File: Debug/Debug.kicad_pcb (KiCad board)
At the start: 4 copper layers, 127 x 88.9 mm, 37 parts, among them J1 Expansion_Connector, SW1 Step, SW2 PHI1/Step, SW3 Run, SW4 SI/SC, U1 74LS04, U10 MC14495P1, U11 HDSP-7803, U12 MC14495P1, U13 HDSP-7803, U14 MC14495P1, U15 HDSP-7803, U2 74LS74, U3 MC14495P1, U4 HDSP-7803, U5 74LS374, U6 MC14495P1, U7 HDSP-7803, U8 MC14495P1, U9 HDSP-7803

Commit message: 98 unrouted traces...
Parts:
- U1: value 74LS04 -> 74HCT04
- U2: value 74LS74 -> 74HCT74
- U5: value 74LS374 -> 74HCT374
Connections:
- J1 pad 1: VCC -> +5V
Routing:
- net GND: track 0.00 -> 601.5 mm
- net ~{IRQ}: track 0.00 -> 60.2 mm, vias 0 -> 2
- net +5V: track 0.00 -> 57.0 mm
- net LE: track 0.00 -> 49.0 mm
- net Net-(SW3-Pad1): track 0.00 -> 14.0 mm
- net Net-(D5-Pad2): track 0.00 -> 7.63 mm, vias 0 -> 1
- net Net-(D4-Pad2): track 0.00 -> 7.63 mm, vias 0 -> 1
- net Net-(D8-Pad2): track 0.00 -> 7.63 mm, vias 0 -> 1
- net Net-(D1-Pad2): track 0.00 -> 7.62 mm, vias 0 -> 1
- net Net-(D6-Pad2): track 0.00 -> 7.62 mm, vias 0 -> 1
- net Net-(D3-Pad2): track 0.00 -> 7.62 mm, vias 0 -> 1
- net Net-(D7-Pad2): track 0.00 -> 7.62 mm, vias 0 -> 1
- net Net-(D2-Pad2): track 0.00 -> 7.62 mm, vias 0 -> 1
- net Net-(SW1-Pad2): track 0.00 -> 6.00 mm
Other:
- outline, holes or cut-outs redrawn

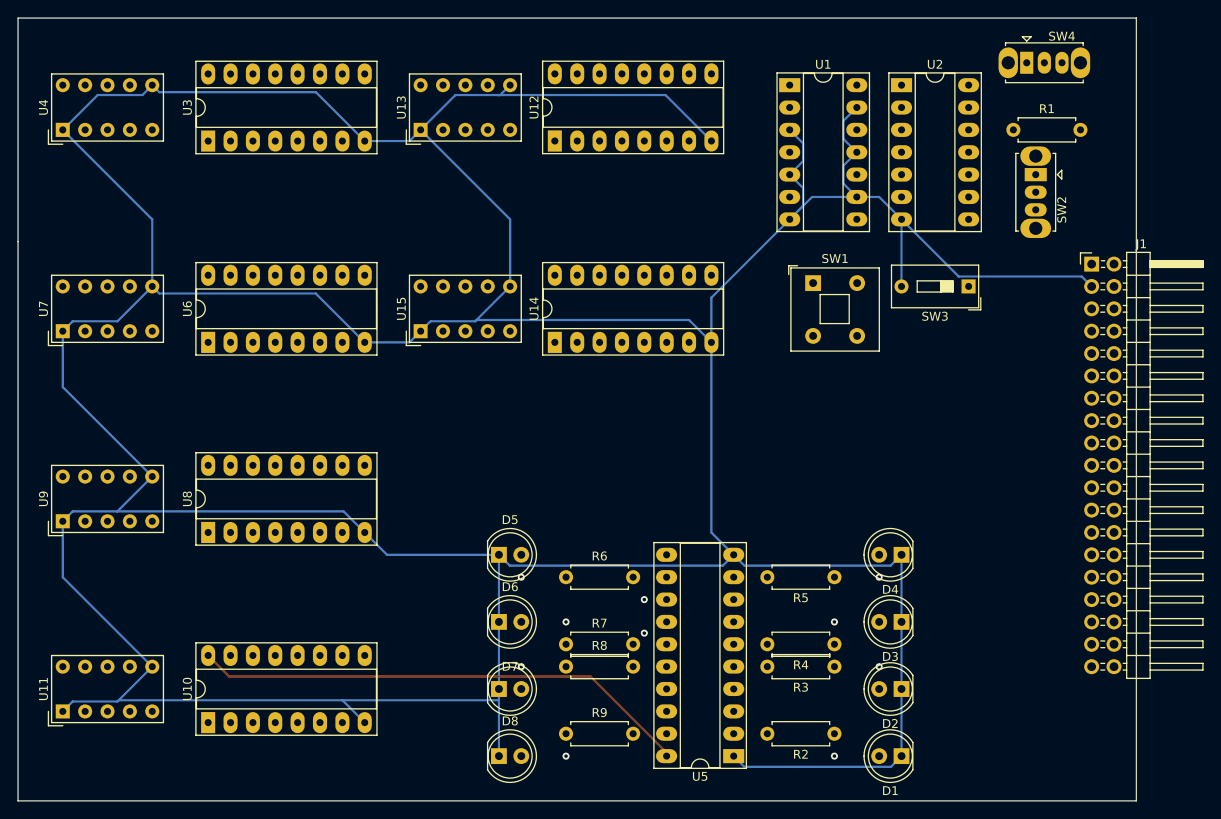
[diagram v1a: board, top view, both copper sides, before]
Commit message: 90 unrouted traces...
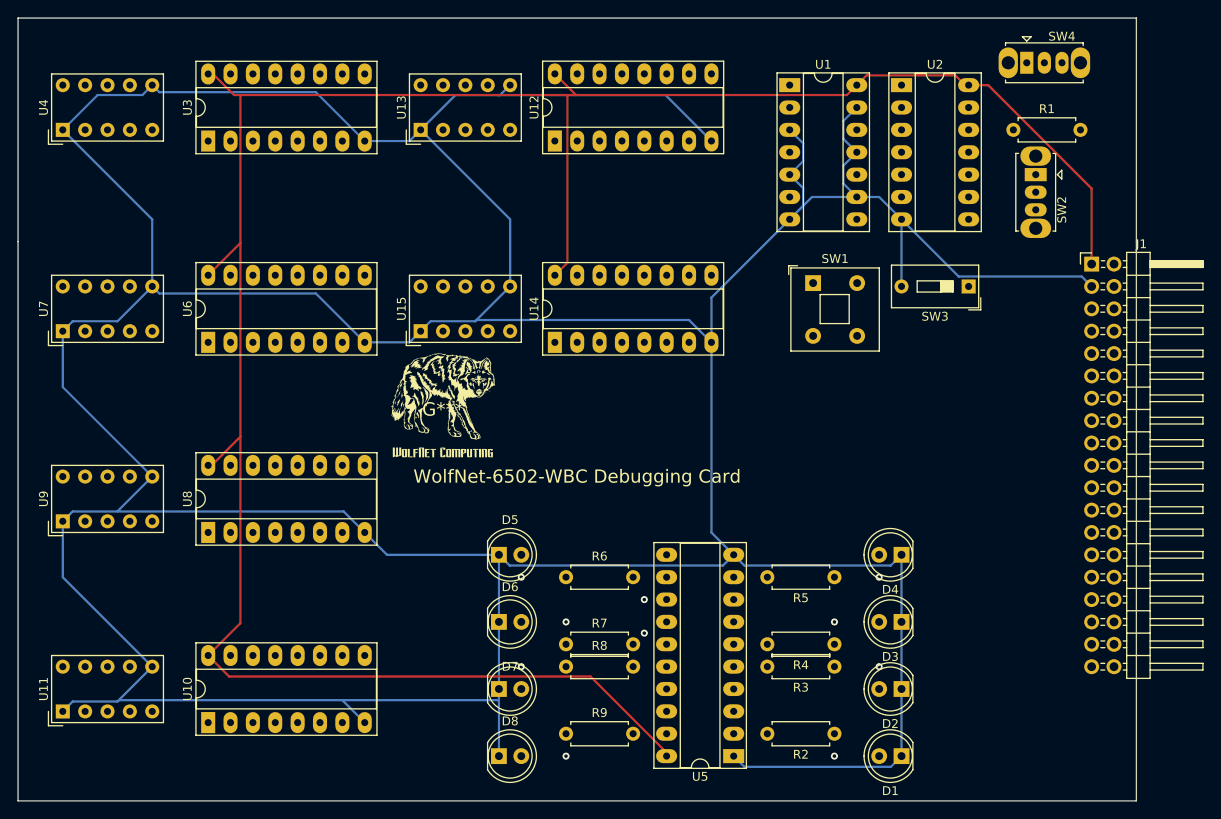
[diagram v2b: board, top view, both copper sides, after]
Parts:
- added G***: LOGO, WolfNet:WolfNet-Logo_silkscreen, F.Cu at (124.5, 69.8)
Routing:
- net +5V: track 57.0 -> 273.0 mm
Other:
- board text added: "WolfNet-6502-WBC Debugging Card"

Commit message: 64 unrouted traces...
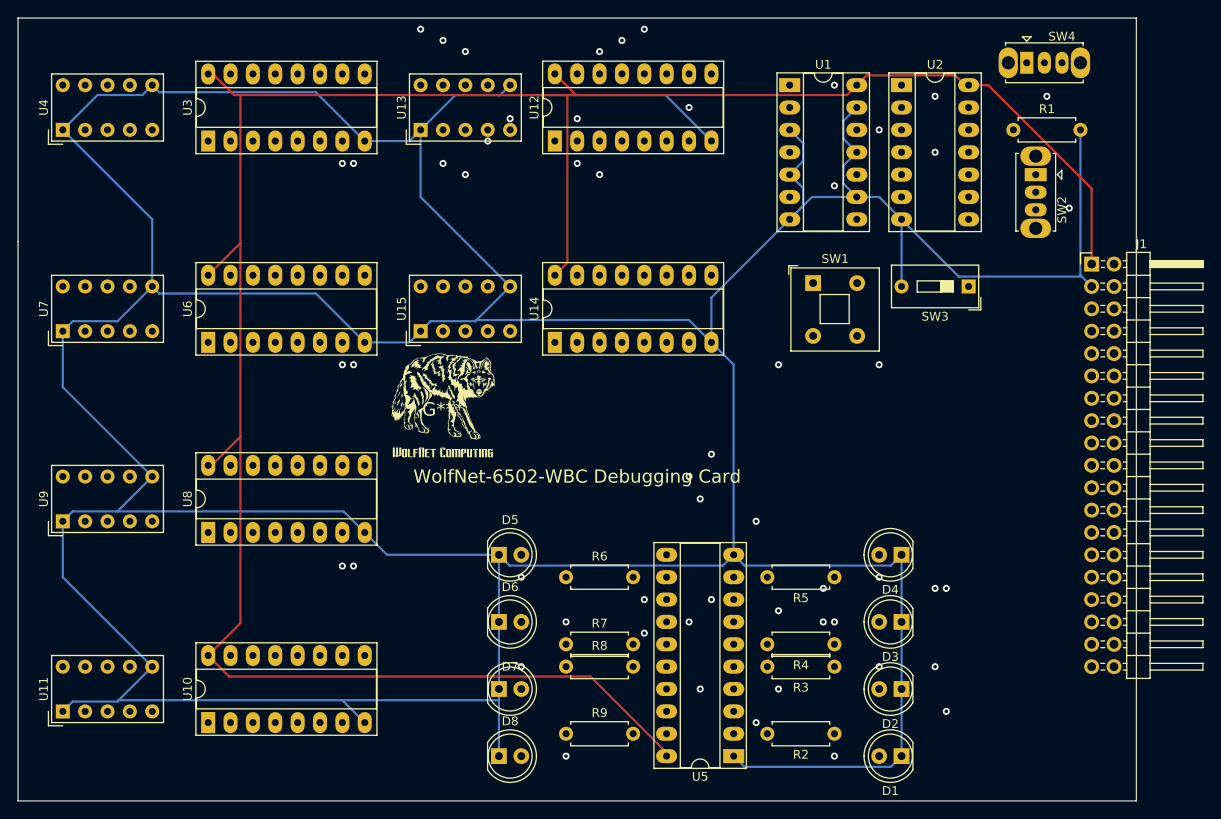
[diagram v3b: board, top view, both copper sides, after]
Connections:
- J1 pad 37: R\~{W} -> R/~{W}
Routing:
- net LE: track 49.0 -> 177.0 mm, vias 0 -> 7
- net SYNC: track 0.00 -> 121.9 mm, vias 0 -> 5
- net PHI1: track 0.00 -> 82.3 mm, vias 0 -> 2
- net PHI2: track 0.00 -> 76.2 mm, vias 0 -> 2
- net CLK: track 0.00 -> 68.6 mm, vias 0 -> 2
- net ~{RESET}: track 0.00 -> 66.0 mm, vias 0 -> 2
- net RDY: track 0.00 -> 58.4 mm, vias 0 -> 2
- net R/~{W}: track 0.00 -> 53.4 mm, vias 0 -> 4
- net Net-(SW2-Pad2): track 0.00 -> 39.7 mm, vias 0 -> 2
- net Net-(U12-Pad12): track 0.00 -> 36.8 mm, vias 0 -> 2
- net Net-(U12-Pad13): track 0.00 -> 29.2 mm, vias 0 -> 2
- net Step: track 0.00 -> 28.8 mm, vias 0 -> 1
- net Net-(SW4-Pad2): track 0.00 -> 26.8 mm, vias 0 -> 3
- net Net-(U12-Pad3): track 0.00 -> 24.1 mm, vias 0 -> 2
- net Net-(U12-Pad2): track 0.00 -> 21.6 mm, vias 0 -> 2
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
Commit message: 59 unrouted traces...
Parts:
- SW3: footprint Button_Switch_THT:SW_DIP_SPSTx01_Slide_9.78x4.72mm_W7.62mm_P2.54mm -> Button_Switch_THT:SW_Slide_1P2T_CK_OS102011MS2Q
- moved SW3 0.73 mm to (184.9, 55.9)
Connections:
- SW3 pad 1: Net-(SW3-Pad1) -> unconnected-(SW3-Pad1)
- SW3 pad 2: GND -> Net-(U2-Pad10)
- U2 pad 10: Net-(SW3-Pad1) -> Net-(U2-Pad10)
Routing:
- net A15: track 0.00 -> 86.8 mm
- net RDY: track 58.4 -> 115.6 mm, vias 2 -> 7
- net Net-(R1-Pad1): track 5.08 -> 45.8 mm, vias 0 -> 4
- net Net-(SW1-Pad1): track 0.00 -> 37.8 mm, vias 0 -> 3
- net Net-(SW1-Pad2): track 6.00 -> 20.8 mm, vias 0 -> 1
- net Net-(SW3-Pad1): track 14.0 -> 0.00 mm
- net Net-(U2-Pad10): track 0.00 -> 13.4 mm
- net GND: track 618.2 -> 613.6 mm

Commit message: 45 unrouted traces...
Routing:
- net D3: track 0.00 -> 89.8 mm, vias 0 -> 3
- net D2: track 0.00 -> 84.2 mm, vias 0 -> 3
- net Net-(U3-Pad12): track 0.00 -> 38.1 mm, vias 0 -> 2
- net PHI1: track 82.3 -> 119.2 mm, vias 2 -> 4
- net Net-(U3-Pad13): track 0.00 -> 30.5 mm, vias 0 -> 2
- net Net-(U3-Pad3): track 0.00 -> 27.9 mm, vias 0 -> 2
- net Net-(U6-Pad3): track 0.00 -> 25.4 mm, vias 0 -> 2
- net Net-(U3-Pad2): track 0.00 -> 25.4 mm, vias 0 -> 2
- net Net-(U3-Pad14): track 0.00 -> 22.9 mm, vias 0 -> 2
- net Net-(U6-Pad2): track 0.00 -> 22.9 mm, vias 0 -> 2
- net Net-(U6-Pad15): track 0.00 -> 15.2 mm, vias 0 -> 2
- net Net-(U3-Pad15): track 0.00 -> 15.2 mm, vias 0 -> 2
- net Net-(U3-Pad1): track 0.00 -> 15.2 mm, vias 0 -> 2
- net Net-(U6-Pad1): track 0.00 -> 10.2 mm, vias 0 -> 1
- net +5V: track 271.3 -> 278.1 mm
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
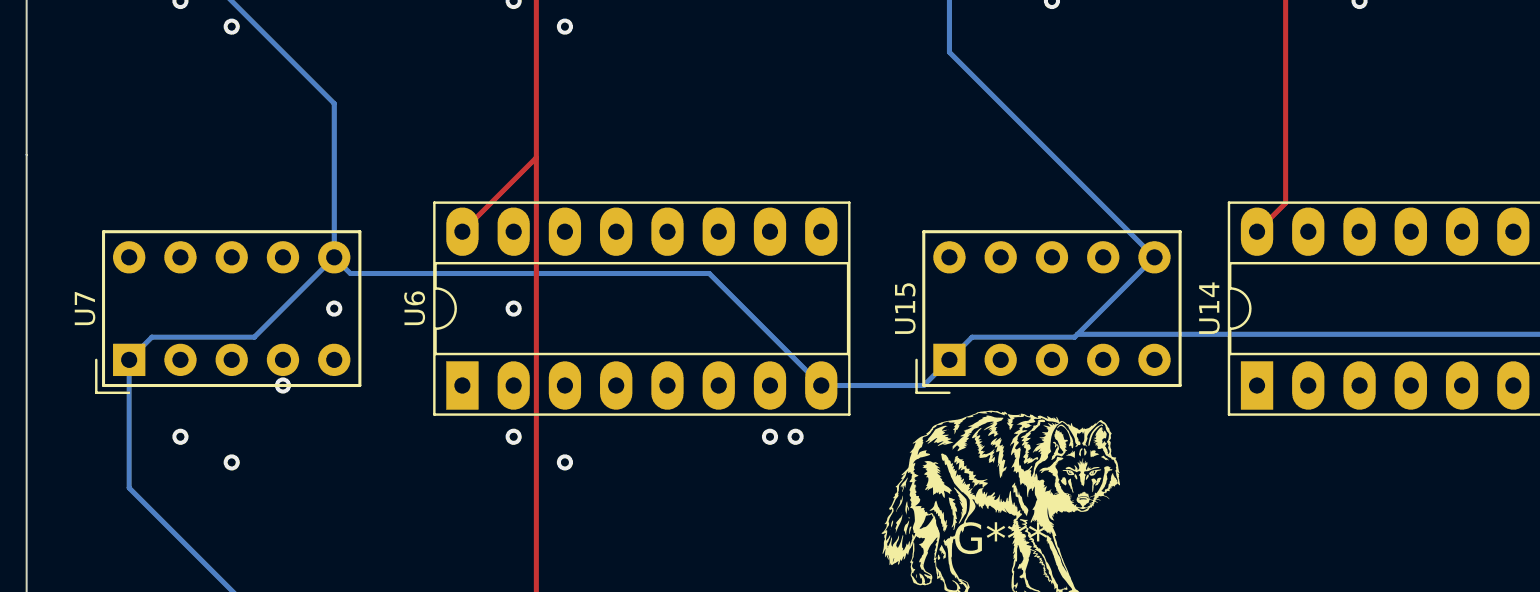
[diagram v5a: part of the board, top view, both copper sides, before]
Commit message: 36 unrouted traces...
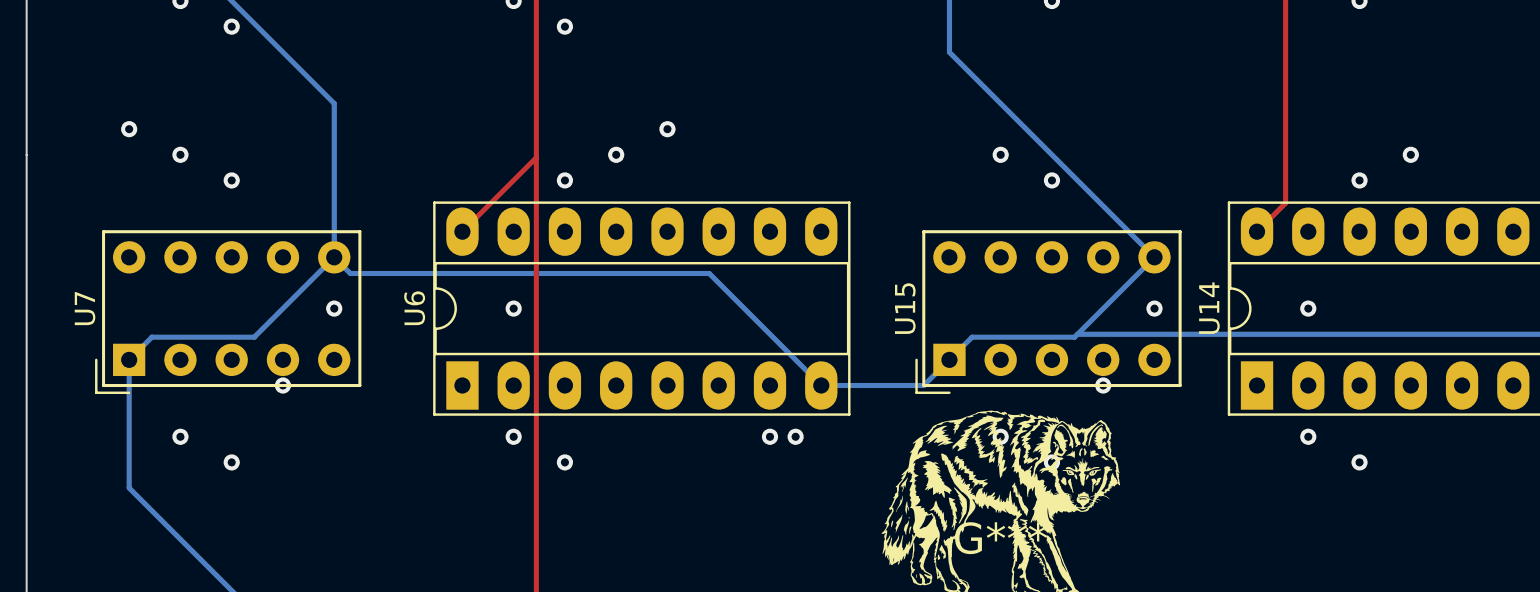
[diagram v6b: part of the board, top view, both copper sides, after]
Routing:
- net Net-(U6-Pad12): track 0.00 -> 38.1 mm, vias 0 -> 2
- net Net-(U6-Pad13): track 0.00 -> 30.5 mm, vias 0 -> 2
- net Net-(U14-Pad13): track 0.00 -> 29.2 mm, vias 0 -> 2
- net Net-(U14-Pad3): track 0.00 -> 24.1 mm, vias 0 -> 2
- net Net-(U6-Pad14): track 0.00 -> 22.9 mm, vias 0 -> 2
- net Net-(U14-Pad14): track 0.00 -> 21.6 mm, vias 0 -> 2
- net Net-(U14-Pad2): track 0.00 -> 21.6 mm, vias 0 -> 2
- net Net-(U14-Pad15): track 0.00 -> 14.0 mm, vias 0 -> 2
- net Net-(U14-Pad1): track 0.00 -> 8.89 mm, vias 0 -> 1
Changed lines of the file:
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@@
   (segment (start 102.87 66.04) (end 102.87 62.23) (width 0.25) (layer "In1.Cu") (net 83))
   (segment (start 86.36 66.04) (end 102.87 66.04) (width 0.25) (layer "In2.Cu") (net 83))
+  (via (at 107.95 49.53) (size 0.8) (drill 0.4) (layers "F.Cu" "B.Cu") (net 86))
+  (via (at 81.28 49.53) (size 0.8) (drill 0.4) (layers "F.Cu" "B.Cu") (net 86))
+  (segment (start 81.28 49.53) (end 81.28 55.88) (width 0.25) (layer "In1.Cu") (net 86))
+  (segment (start 107.95 54.61) (end 107.95 49.53) (width 0.25) (layer "In1.Cu") (net 86))
+  (segment (start 107.95 49.53) (end 81.28 49.53) (width 0.25) (layer "In2.Cu") (net 86))
+  (via (at 105.41 50.8) (size 0.8) (drill 0.4) (layers "F.Cu" "B.Cu") (net 87))
+  (via (at 83.82 50.8) (size 0.8) (drill 0.4) (layers "F.Cu" "B.Cu") (net 87))
+  (segment (start 105.41 50.8) (end 105.41 54.61) (width 0.25) (layer "In1.Cu") (net 87))
+  (segment (start 83.82 55.88) (end 83.82 50.8) (width 0.25) (layer "In1.Cu") (net 87))
+  (segment (start 83.82 50.8) (end 105.41 50.8) (width 0.25) (layer "In2.Cu") (net 87))
+  (via (at 102.87 52.07) (size 0.8) (drill 0.4) (layers "F.Cu" "B.Cu") (net 88))
+  (via (at 86.36 52.07) (size 0.8) (drill 0.4) (layers "F.Cu" "B.Cu") (net 88))
+  (segment (start 102.87 54.61) (end 102.87 52.07) (width 0.25) (layer "In1.Cu") (net 88))
+  (segment (start 86.36 52.07) (end 86.36 55.88) (width 0.25) (layer "In1.Cu") (net 88))
+  (segment (start 102.87 52.07) (end 86.36 52.07) (width 0.25) (layer "In2.Cu") (net 88))
   (via (at 91.44 58.42) (size 0.8) (drill 0.4) (layers "F.Cu" "B.Cu") (net 89))
   (via (at 100.33 58.42) (size 0.8) (drill 0.4) (layers "F.Cu" "B.Cu") (net 89))
@@
   (segment (start 139.7 31.74) (end 139.7 36.83) (width 0.25) (layer "In1.Cu") (net 119))
   (segment (start 139.7 36.83) (end 132.08 36.83) (width 0.25) (layer "In2.Cu") (net 119))
+  (via (at 129.54 62.23) (size 0.8) (drill 0.4) (layers "F.Cu" "B.Cu") (net 121))
+  (segment (start 129.54 62.23) (end 129.54 60.96) (width 0.25) (layer "In1.Cu") (net 121))
+  (segment (start 137.16 62.23) (end 129.54 62.23) (width 0.25) (layer "In2.Cu") (net 121))
+  (via (at 124.46 64.77) (size 0.8) (drill 0.4) (layers "F.Cu" "B.Cu") (net 122))
+  (via (at 139.7 64.77) (size 0.8) (drill 0.4) (layers "F.Cu" "B.Cu") (net 122))
+  (segment (start 139.7 62.23) (end 139.7 64.77) (width 0.25) (layer "In1.Cu") (net 122))
+  (segment (start 124.46 64.77) (end 124.46 60.96) (width 0.25) (layer "In1.Cu") (net 122))
+  (segment (start 139.7 64.77) (end 124.46 64.77) (width 0.25) (layer "In2.Cu") (net 122))
+  (via (at 142.24 66.04) (size 0.8) (drill 0.4) (layers "F.Cu" "B.Cu") (net 123))
+  (via (at 127 66.04) (size 0.8) (drill 0.4) (layers "F.Cu" "B.Cu") (net 123))
+  (segment (start 142.24 66.04) (end 142.24 62.23) (width 0.25) (layer "In1.Cu") (net 123))
+  (segment (start 127 60.96) (end 127 66.04) (width 0.25) (layer "In1.Cu") (net 123))
+  (segment (start 127 66.04) (end 142.24 66.04) (width 0.25) (layer "In2.Cu") (net 123))
+  (via (at 124.46 50.8) (size 0.8) (drill 0.4) (layers "F.Cu" "B.Cu") (net 127))
+  (via (at 144.78 50.8) (size 0.8) (drill 0.4) (layers "F.Cu" "B.Cu") (net 127))
+  (segment (start 124.46 55.88) (end 124.46 50.8) (width 0.25) (layer "In1.Cu") (net 127))
+  (segment (start 144.78 50.8) (end 144.78 54.61) (width 0.25) (layer "In1.Cu") (net 127))
+  (segment (start 124.46 50.8) (end 144.78 50.8) (width 0.25) (layer "In2.Cu") (net 127))
+  (via (at 142.24 52.07) (size 0.8) (drill 0.4) (layers "F.Cu" "B.Cu") (net 128))
+  (via (at 127 52.07) (size 0.8) (drill 0.4) (layers "F.Cu" "B.Cu") (net 128))
+  (segment (start 142.24 54.61) (end 142.24 52.07) (width 0.25) (layer "In1.Cu") (net 128))
+  (segment (start 127 52.07) (end 127 55.88) (width 0.25) (layer "In1.Cu") (net 128))
+  (segment (start 142.24 52.07) (end 127 52.07) (width 0.25) (layer "In2.Cu") (net 128))
+  (via (at 139.7 58.42) (size 0.8) (drill 0.4) (layers "F.Cu" "B.Cu") (net 129))
+  (via (at 132.08 58.42) (size 0.8) (drill 0.4) (layers "F.Cu" "B.Cu") (net 129))
+  (segment (start 132.08 58.42) (end 132.08 60.96) (width 0.25) (layer "In1.Cu") (net 129))
+  (segment (start 139.7 54.61) (end 139.7 58.42) (width 0.25) (layer "In1.Cu") (net 129))
+  (segment (start 139.7 58.42) (end 132.08 58.42) (width 0.25) (layer "In2.Cu") (net 129))
   (segment (start 182.62548 55.12548) (end 182.62548 44.70452) (width 0.25) (layer "In1.Cu") (net 132))
   (segment (start 182.62548 44.70452) (end 184.15 43.18) (width 0.25) (layer "In1.Cu") (net 132))

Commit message: Completed debugging card...
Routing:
- net A3: track 0.00 -> 121.2 mm, vias 0 -> 3
- net A2: track 0.00 -> 112.8 mm, vias 0 -> 3
- net A0: track 0.00 -> 112.1 mm, vias 0 -> 1
- net A1: track 0.00 -> 111.6 mm, vias 0 -> 3
- net A7: track 0.00 -> 107.9 mm, vias 0 -> 3
- net A12: track 0.00 -> 106.9 mm, vias 0 -> 1
- net A14: track 0.00 -> 105.2 mm, vias 0 -> 4
- net A11: track 0.00 -> 102.1 mm, vias 0 -> 3
- net A6: track 0.00 -> 100.9 mm, vias 0 -> 1
- net A13: track 0.00 -> 100.1 mm, vias 0 -> 1
- net A10: track 0.00 -> 97.3 mm, vias 0 -> 3
- net A5: track 0.00 -> 97.2 mm, vias 0 -> 1
- net A4: track 0.00 -> 96.5 mm, vias 0 -> 1
- net A8: track 0.00 -> 95.2 mm, vias 0 -> 1
- net A9: track 0.00 -> 90.2 mm, vias 0 -> 1
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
